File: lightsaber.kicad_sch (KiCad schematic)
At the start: 7 parts, among them SW1 SW_Push, SW3 POWER, U1 C3 Pico

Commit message: Preliminary PCB layout
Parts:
- removed LIN1: LEDs_In, neopixel-strip:neopixel-strip, symbol neopixel-strip:LEDs_In
- added R1: VT93xx, OptoDevice:R_LDR_4.9x4.2mm_P2.54mm_Vertical, symbol Sensor_Optical:VT93xx
- added R3: R, Resistor_SMD:R_0805_2012Metric_Pad1.20x1.40mm_HandSolder, symbol Device:R
- SW1: value SW_Push -> Button
- renumbered LOUT1 to NP1
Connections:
- net GND: now reaches SW1.1
- net GND: now also BT1.2 (-), NP1.3 (GND), R2.3, U1.2 (GND), R1.2
- net Button: now reaches SW1.2
- net Button: now also U1.11 (IO4/MOSI)
- net +5V: now reaches U1.1 (5V)
- net Light: now reaches U1.10 (IO5)
- net Light: now also R1.1, R3.2
- net Poti: now reaches U1.13 (IO1/SCK)
- net Poti: now also R2.2
- net Neopixel: now reaches U1.14 (IO2)
- net Neopixel: now also NP1.2 (Data)
- net +4V: now reaches U1.15 (IO3/VBAT)
- net +4V: now also BT1.1 (+), NP1.1 (VCC)
- net Power: now reaches U1.16 (RST/EN)
- net Power: now also SW3.3 (C)
- net +3V3: now reaches U1.9 (3V3)
- net +3V3: now also R2.1, SW3.2 (B), R3.1
- no-connect marks 0 -> 8
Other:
- moved on the sheet: BT1, NP1, R2, SW1, SW3

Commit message: Update PCB for Lightsaber
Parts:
- added TP1: TO-BAT, TestPoint:TestPoint_Loop_D2.50mm_Drill1.0mm, symbol Connector:TestPoint
- R3: value R -> 100k
- SW2: renamed from SW3; footprint as12ap:as12ap -> Button_Switch_SMD:SW_SPDT_CK_JS102011SAQN
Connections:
- net +3V3: no longer SW2.2 (B)
- net +4V: now also SW2.3 (C), TP1.1; no longer BT1.1 (+), U1.15 (IO3/VBAT)
- net Power: no longer names the net of U1.16 (RST/EN)
- net Power: no longer SW2.3 (C)
- new net VBAT: BT1.1 (+), SW2.2 (B)
- no-connect marks 8 -> 10
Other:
- moved on the sheet: SW2

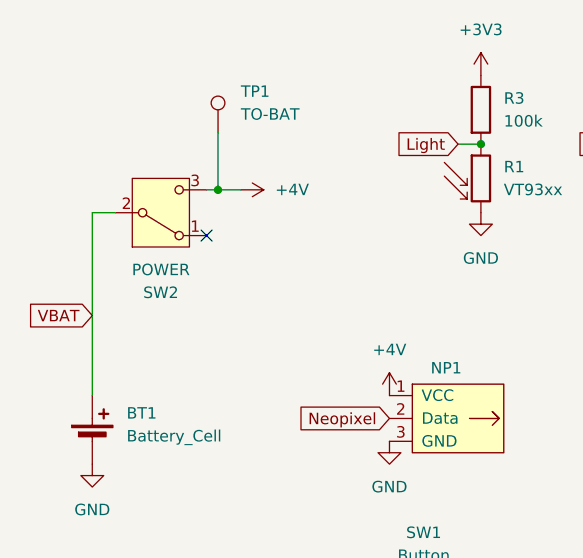
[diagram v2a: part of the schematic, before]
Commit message: Fixed switch between 5V and V_Batt
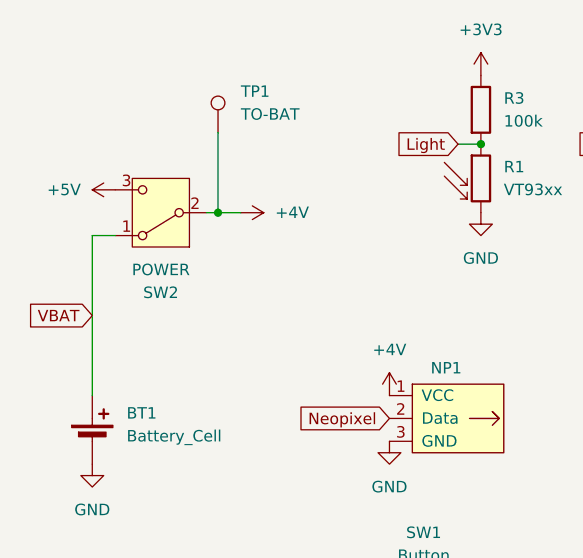
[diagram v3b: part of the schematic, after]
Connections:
- net +4V: now also SW2.2 (B); no longer SW2.3 (C)
- net +5V: now also SW2.3 (C)
- net VBAT: now also SW2.1 (A); no longer SW2.2 (B)
- no-connect marks 10 -> 9
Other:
- moved on the sheet: SW2
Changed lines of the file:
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@@
 	)
 	(junction
-		(at 40.64 35.56)
+		(at 40.64 38.1)
 		(diameter 0)
 		(color 0 0 0 0)
@@
 	(no_connect
 		(at 105.41 55.88)
-	)
-	(no_connect
-		(at 39.37 40.64)
 	)
 	(no_connect
@@
 	(wire
 		(pts
-			(xy 26.67 58.42) (xy 26.67 38.1)
+			(xy 40.64 29.21) (xy 40.64 38.1)
 		)
 		(stroke
@@
 	(wire
 		(pts
-			(xy 43.18 35.56) (xy 40.64 35.56)
+			(xy 26.67 58.42) (xy 26.67 40.64)
 		)
 		(stroke
@@
 	(wire
 		(pts
-			(xy 40.64 29.21) (xy 40.64 35.56)
+			(xy 43.18 38.1) (xy 40.64 38.1)
 		)
 		(stroke
@@
 	(wire
 		(pts
-			(xy 39.37 35.56) (xy 40.64 35.56)
+			(xy 39.37 38.1) (xy 40.64 38.1)
 		)
 		(stroke
@@
 	(wire
 		(pts
-			(xy 26.67 38.1) (xy 29.21 38.1)
+			(xy 26.67 40.64) (xy 29.21 40.64)
 		)
 		(stroke
@@
 	(symbol
 		(lib_id "power:+4V")
-		(at 43.18 35.56 270)
+		(at 43.18 38.1 270)
 		(unit 1)
 		(exclude_from_sim no)
@@
 		(fields_autoplaced yes)
 		(property "Reference" "#PWR03"
-			(at 39.37 35.56 0)
+			(at 39.37 38.1 0)
 			(effects
 				(font
@@
 		)
 		(property "Value" "+4V"
-			(at 46.99 35.5599 90)
+			(at 46.99 38.0999 90)
 			(effects
 				(font
@@
 		)
 		(property "Footprint" ""
-			(at 43.18 35.56 0)
+			(at 43.18 38.1 0)
 			(effects
 				(font
@@
 		)
 		(property "Datasheet" ""
-			(at 43.18 35.56 0)
+			(at 43.18 38.1 0)
 			(effects
 				(font
@@
 		)
 		(property "Description" "Power symbol creates a global label with name \"+4V\""
-			(at 43.18 35.56 0)
+			(at 43.18 38.1 0)
 			(effects
 				(font
@@
 				(path "/be5e5df5-91f4-4b4d-9714-13949d1f37c8"
 					(reference "#PWR03")
+					(unit 1)
+				)
+			)
+		)
+	)
+	(symbol
+		(lib_id "power:+5V")
+		(at 29.21 35.56 90)
+		(unit 1)
+		(exclude_from_sim no)
+		(in_bom yes)
+		(on_board yes)
+		(dnp no)
+		(fields_autoplaced yes)
+		(property "Reference" "#PWR06"
+			(at 33.02 35.56 0)
+			(effects
+				(font
+					(size 1.27 1.27)
+				)
+				(hide yes)
+			)
+		)
+		(property "Value" "+5V"
+			(at 25.4 35.5599 90)
+			(effects
+				(font
+					(size 1.27 1.27)
+				)
+				(justify left)
+			)
+		)
+		(property "Footprint" ""
+			(at 29.21 35.56 0)
+			(effects
+				(font
+					(size 1.27 1.27)
+				)
+				(hide yes)
+			)
+		)
+		(property "Datasheet" ""
+			(at 29.21 35.56 0)
+			(effects
+				(font
+					(size 1.27 1.27)
+				)
+				(hide yes)
+			)
+		)
+		(property "Description" "Power symbol creates a global label with name \"+5V\""
+			(at 29.21 35.56 0)
+			(effects
+				(font
+					(size 1.27 1.27)
+				)
+				(hide yes)
+			)
+		)
+		(pin "1"
+		)
+		(instances
+			(project "lightsaber"
+				(path "/be5e5df5-91f4-4b4d-9714-13949d1f37c8"
+					(reference "#PWR06")
 					(unit 1)
 				)
@@
 	(symbol
 		(lib_id "Switch:SW_SPDT")
-		(at 34.29 38.1 0)
-		(mirror x)
-		(unit 1)
-		(exclude_from_sim no)
+		(at 34.29 38.1 180)
+		(unit 1)
+		(exclude_from_sim no)

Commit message: Make sure that the neopixel does not drain the battery so use 3V3 instead of VBAT
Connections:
- net +3V3: now also NP1.1 (VCC)
- net +4V: no longer NP1.1 (VCC)

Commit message: Specify light sensor and its resistor
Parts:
- R1: footprint OptoDevice:R_LDR_4.9x4.2mm_P2.54mm_Vertical -> OptoDevice:R_LDR_5.1x4.3mm_P3.4mm_Vertical
- R3: value 100k -> 47k
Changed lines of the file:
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@@
 			)
 		)
-		(property "Value" "100k"
+		(property "Value" "47k"
 			(at 72.39 27.9399 0)
 			(effects
@@
 			)
 		)
-		(property "Footprint" "OptoDevice:R_LDR_4.9x4.2mm_P2.54mm_Vertical"
+		(property "Footprint" "OptoDevice:R_LDR_5.1x4.3mm_P3.4mm_Vertical"
 			(at 74.295 34.29 90)
 			(effects

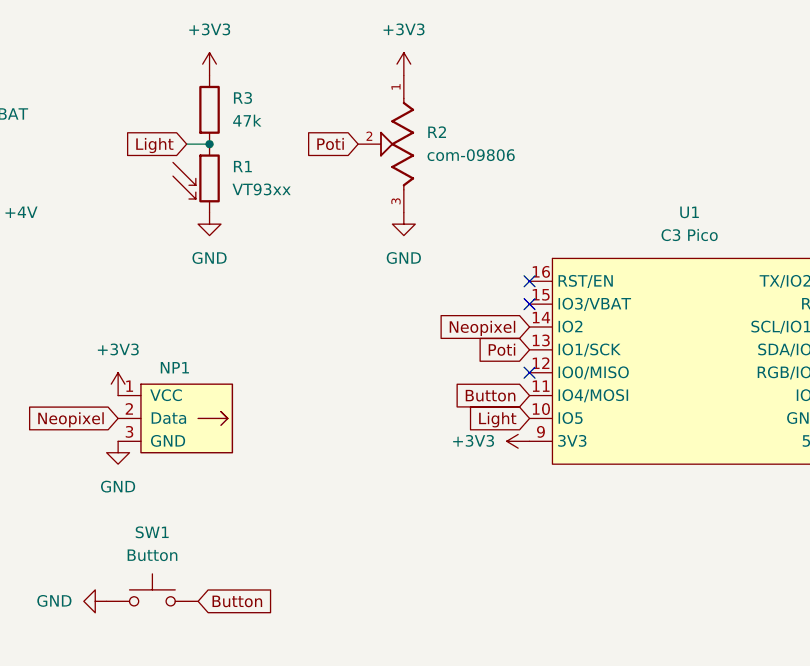
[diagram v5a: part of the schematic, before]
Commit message: Change pinout, add m3 mounting holes
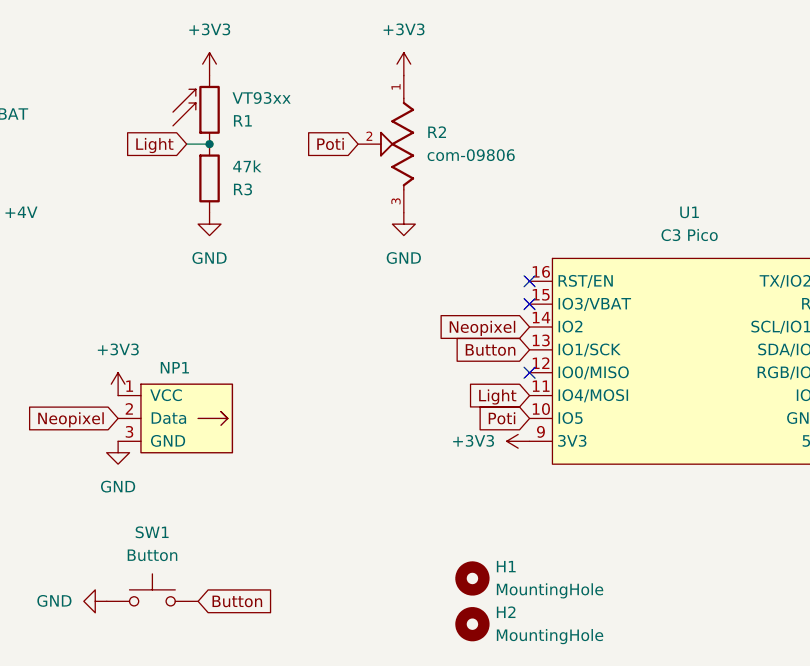
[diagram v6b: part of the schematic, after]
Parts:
- added H1, H2: MountingHole, MountingHole:MountingHole_3.2mm_M3, symbol Mechanical:MountingHole
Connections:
- net +3V3: now also R1.2; no longer R3.1
- net Button: now also U1.13 (IO1/SCK); no longer U1.11 (IO4/MOSI)
- net GND: now also R3.1; no longer R1.2
- net Light: now also U1.11 (IO4/MOSI); no longer U1.10 (IO5)
- net Poti: now also U1.10 (IO5); no longer U1.13 (IO1/SCK)
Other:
- moved on the sheet: R1, R3
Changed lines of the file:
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@@
 	(global_label "Light"
 		(shape input)
-		(at 105.41 60.96 180)
+		(at 105.41 58.42 180)
 		(fields_autoplaced yes)
 		(effects
@@
 		)
 		(property "Intersheetrefs" "${INTERSHEET_REFS}"
-			(at 97.7682 60.96 0)
+			(at 97.7682 58.42 0)
 			(effects
 				(font
@@
 	(global_label "Poti"
 		(shape input)
-		(at 105.41 53.34 180)
+		(at 105.41 60.96 180)
 		(fields_autoplaced yes)
 		(effects
@@
 		)
 		(property "Intersheetrefs" "${INTERSHEET_REFS}"
-			(at 98.6753 53.34 0)
+			(at 98.6753 60.96 0)
 			(effects
 				(font
@@
 	(global_label "Button"
 		(shape input)
-		(at 105.41 58.42 180)
+		(at 105.41 53.34 180)
 		(fields_autoplaced yes)
 		(effects
@@
 		)
 		(property "Intersheetrefs" "${INTERSHEET_REFS}"
-			(at 96.2564 58.42 0)
+			(at 96.2564 53.34 0)
 			(effects
 				(font
@@
 	(symbol
 		(lib_id "Device:R")
-		(at 69.85 26.67 0)
+		(at 69.85 34.29 0)
+		(mirror x)
 		(unit 1)
 		(exclude_from_sim no)
@@
 		(fields_autoplaced yes)
 		(property "Reference" "R3"
-			(at 72.39 25.3999 0)
+			(at 72.39 35.5601 0)
 			(effects
 				(font
@@
 		)
 		(property "Value" "47k"
-			(at 72.39 27.9399 0)
+			(at 72.39 33.0201 0)
 			(effects
 				(font
@@
 		)
 		(property "Footprint" "Resistor_SMD:R_0805_2012Metric_Pad1.20x1.40mm_HandSolder"
-			(at 68.072 26.67 90)
+			(at 68.072 34.29 90)
 			(effects
 				(font
@@
 		)
 		(property "Datasheet" "~"
-			(at 69.85 26.67 0)
+			(at 69.85 34.29 0)
 			(effects
 				(font
@@
 		)
 		(property "Description" "Resistor"
-			(at 69.85 26.67 0)
+			(at 69.85 34.29 0)
 			(effects
 				(font
@@
 	)
 	(symbol
+		(lib_id "Mechanical:MountingHole")
+		(at 99.06 78.74 0)
+		(unit 1)
+		(exclude_from_sim yes)
+		(in_bom no)
+		(on_board yes)
+		(dnp no)
+		(fields_autoplaced yes)
+		(property "Reference" "H1"
+			(at 101.6 77.4699 0)
+			(effects
+				(font
+					(size 1.27 1.27)
+				)
+				(justify left)
+			)
+		)
+		(property "Value" "MountingHole"
+			(at 101.6 80.0099 0)
+			(effects
+				(font
+					(size 1.27 1.27)
+				)
+				(justify left)
+			)
+		)
+		(property "Footprint" "MountingHole:MountingHole_3.2mm_M3"
+			(at 99.06 78.74 0)
+			(effects
+				(font
+					(size 1.27 1.27)
+				)
+				(hide yes)
+			)
+		)
+		(property "Datasheet" "~"
+			(at 99.06 78.74 0)
+			(effects
+				(font
+					(size 1.27 1.27)
+				)
+				(hide yes)
+			)
+		)
+		(property "Description" "Mounting Hole without connection"
+			(at 99.06 78.74 0)
+			(effects
+				(font
+					(size 1.27 1.27)
+				)
+				(hide yes)
+			)
+		)
+		(instances
+			(project ""
+				(path "/be5e5df5-91f4-4b4d-9714-13949d1f37c8"
+					(reference "H1")
+					(unit 1)
+				)
+			)
+		)
+	)
+	(symbol
 		(lib_id "power:+3V3")
 		(at 91.44 22.86 0)
@@
 	(symbol
 		(lib_id "Sensor_Optical:VT93xx")
-		(at 69.85 34.29 0)
+		(at 69.85 26.67 0)
+		(mirror x)
 		(unit 1)
 		(exclude_from_sim no)
@@
 		(fields_autoplaced yes)
 		(property "Reference" "R1"
-			(at 72.39 33.0199 0)
+			(at 72.39 27.9401 0)
 			(effects
 				(font
@@
 		)
 		(property "Value" "VT93xx"
-			(at 72.39 35.5599 0)
+			(at 72.39 25.4001 0)
 			(effects
 				(font
@@
 		)
 		(property "Footprint" "OptoDevice:R_LDR_5.1x4.3mm_P3.4mm_Vertical"
-			(at 74.295 34.29 90)
+			(at 74.295 26.67 90)
 			(effects
 				(font
@@
 		)
 		(property "Datasheet" "http://www.produktinfo.conrad.com/datenblaetter/125000-149999/140375-da-01-en-FOTOWIDERSTAND__VT_93_N2__THT_.pdf"
-			(at 69.85 35.56 0)
+			(at 69.85 25.4 0)
 			(effects
 				(font
@@
 		)
 		(property "Description" "light dependent resistor"
-			(at 69.85 34.29 0)
+			(at 69.85 26.67 0)
 			(effects
 				(font
@@
 					(unit 1)
 				)
+			)
+		)
+	)
+	(symbol
+		(lib_id "Mechanical:MountingHole")
+		(at 99.06 83.82 0)
+		(unit 1)
+		(exclude_from_sim yes)
+		(in_bom no)
+		(on_board yes)
+		(dnp no)
+		(fields_autoplaced yes)
+		(property "Reference" "H2"
+			(at 101.6 82.5499 0)
+			(effects
+				(font
+					(size 1.27 1.27)
+				)
+				(justify left)
+			)
+		)
+		(property "Value" "MountingHole"
+			(at 101.6 85.0899 0)
+			(effects
+				(font
+					(size 1.27 1.27)
+				)
+				(justify left)
+			)
+		)
+		(property "Footprint" "MountingHole:MountingHole_3.2mm_M3"
+			(at 99.06 83.82 0)
+			(effects
+				(font
+					(size 1.27 1.27)
+				)
+				(hide yes)
+			)
+		)
+		(property "Datasheet" "~"
+			(at 99.06 83.82 0)
+			(effects
+				(font
+					(size 1.27 1.27)
+				)
+				(hide yes)
+			)
+		)
+		(property "Description" "Mounting Hole without connection"
+			(at 99.06 83.82 0)
+			(effects
+				(font
+					(size 1.27 1.27)
+				)
+				(hide yes)
+			)
+		)
+		(instances
+			(project "lightsaber"
+				(path "/be5e5df5-91f4-4b4d-9714-13949d1f37c8"
+					(reference "H2")
+					(unit 1)
+				)

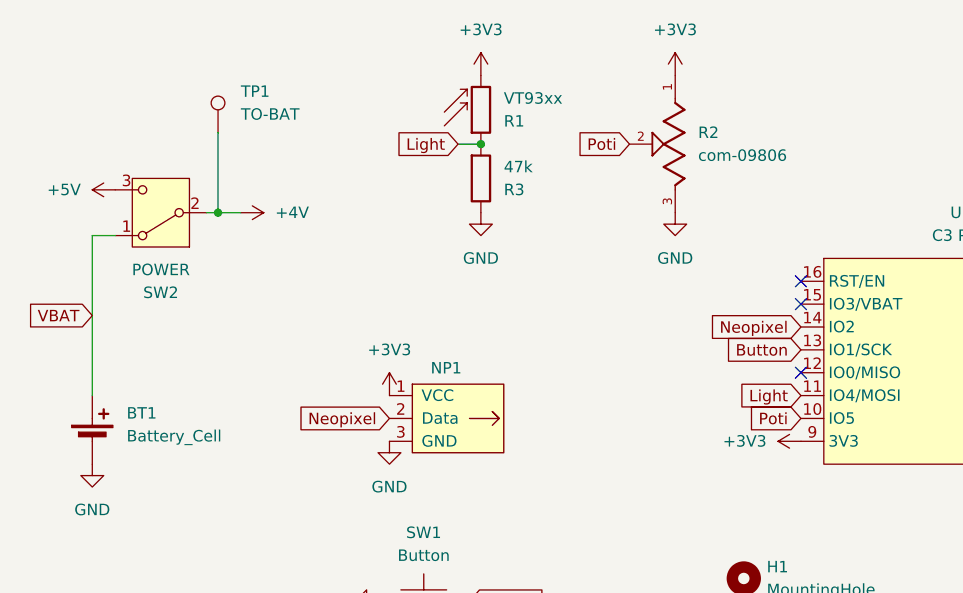
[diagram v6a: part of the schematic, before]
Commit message: Reverse the polarity of the slide switch
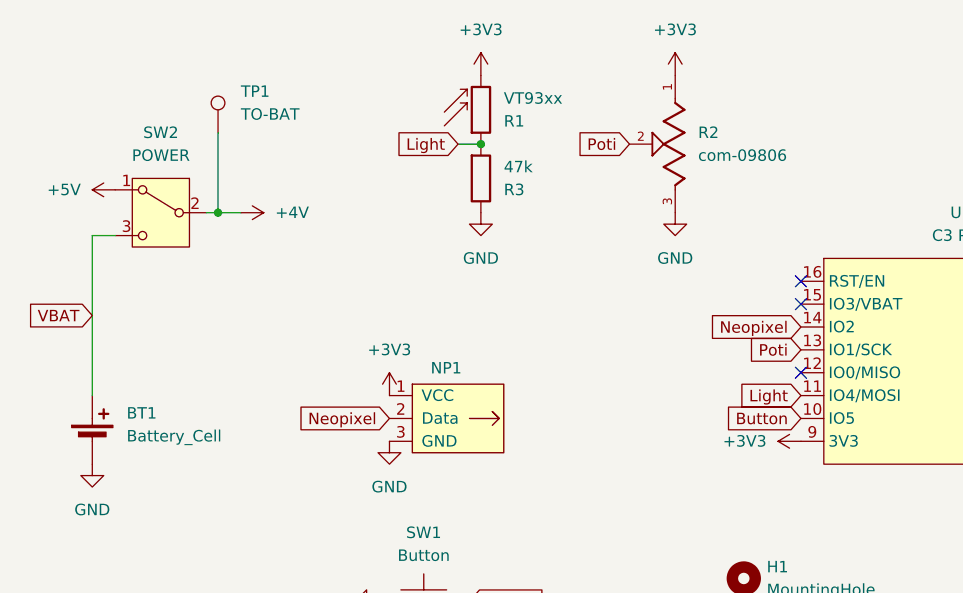
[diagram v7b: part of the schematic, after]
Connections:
- net +5V: now also SW2.1 (A); no longer SW2.3 (C)
- net Button: now also U1.10 (IO5); no longer U1.13 (IO1/SCK)
- net Poti: now also U1.13 (IO1/SCK); no longer U1.10 (IO5)
- net VBAT: now also SW2.3 (C); no longer SW2.1 (A)
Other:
- moved on the sheet: SW2
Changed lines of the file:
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@@
 	(global_label "Poti"
 		(shape input)
-		(at 105.41 60.96 180)
+		(at 105.41 53.34 180)
 		(fields_autoplaced yes)
 		(effects
@@
 		)
 		(property "Intersheetrefs" "${INTERSHEET_REFS}"
-			(at 98.6753 60.96 0)
+			(at 98.6753 53.34 0)
 			(effects
 				(font
@@
 	(global_label "Button"
 		(shape input)
-		(at 105.41 53.34 180)
+		(at 105.41 60.96 180)
 		(fields_autoplaced yes)
 		(effects
@@
 		)
 		(property "Intersheetrefs" "${INTERSHEET_REFS}"
-			(at 96.2564 53.34 0)
+			(at 96.2564 60.96 0)
 			(effects
 				(font
@@
 	(symbol
 		(lib_id "Switch:SW_SPDT")
-		(at 34.29 38.1 180)
+		(at 34.29 38.1 0)
+		(mirror y)
 		(unit 1)
 		(exclude_from_sim no)
@@
 		(dnp no)
 		(property "Reference" "SW2"
-			(at 34.29 46.99 0)
+			(at 34.29 29.21 0)
 			(effects
 				(font
@@
 		)
 		(property "Value" "POWER"
-			(at 34.29 44.45 0)
-			(effects
-				(font
+			(at 34.29 31.75 0)
+			(effects
+				(font

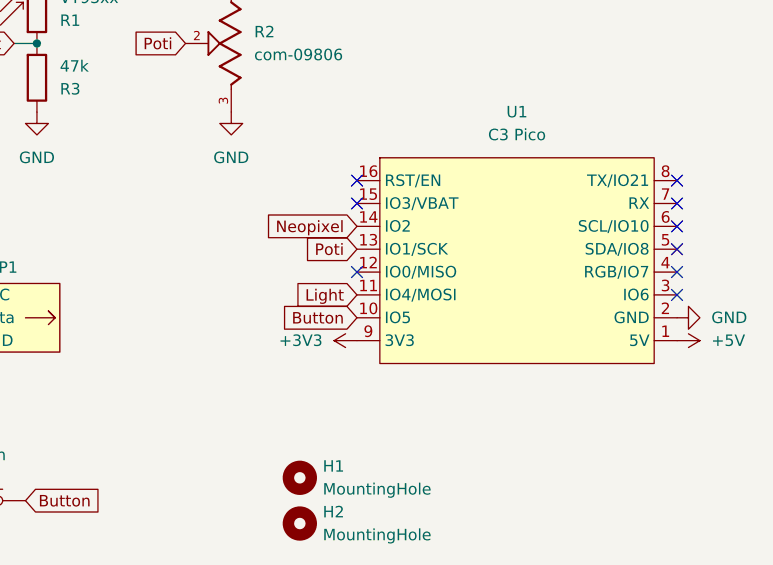
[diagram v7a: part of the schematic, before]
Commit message: Denote the ADC pins
And change the pinout for the light sensor
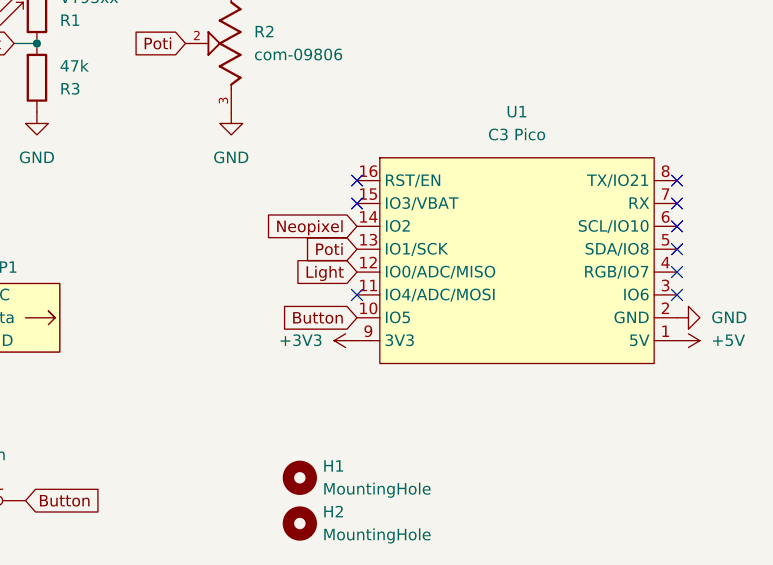
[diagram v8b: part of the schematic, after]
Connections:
- net Light: now also U1.12 (IO0/ADC/MISO); no longer U1.11 (IO4/MOSI)
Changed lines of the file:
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@@
-	)
-	(no_connect
-		(at 105.41 55.88)
 	)
 	(no_connect
@@
 	(no_connect
 		(at 140.97 53.34)
+	)
+	(no_connect
+		(at 105.41 58.42)
 	)
 	(wire
@@
 	(global_label "Light"
 		(shape input)
-		(at 105.41 58.42 180)
+		(at 105.41 55.88 180)
 		(fields_autoplaced yes)
 		(effects
@@
 		)
 		(property "Intersheetrefs" "${INTERSHEET_REFS}"
-			(at 97.7682 58.42 0)
+			(at 97.7682 55.88 0)
 			(effects
 				(font
